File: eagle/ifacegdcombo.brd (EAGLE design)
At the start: 95.8 x 108.5 mm, 35 parts, among them K1 G5V-2, X4 BU-SMA-V

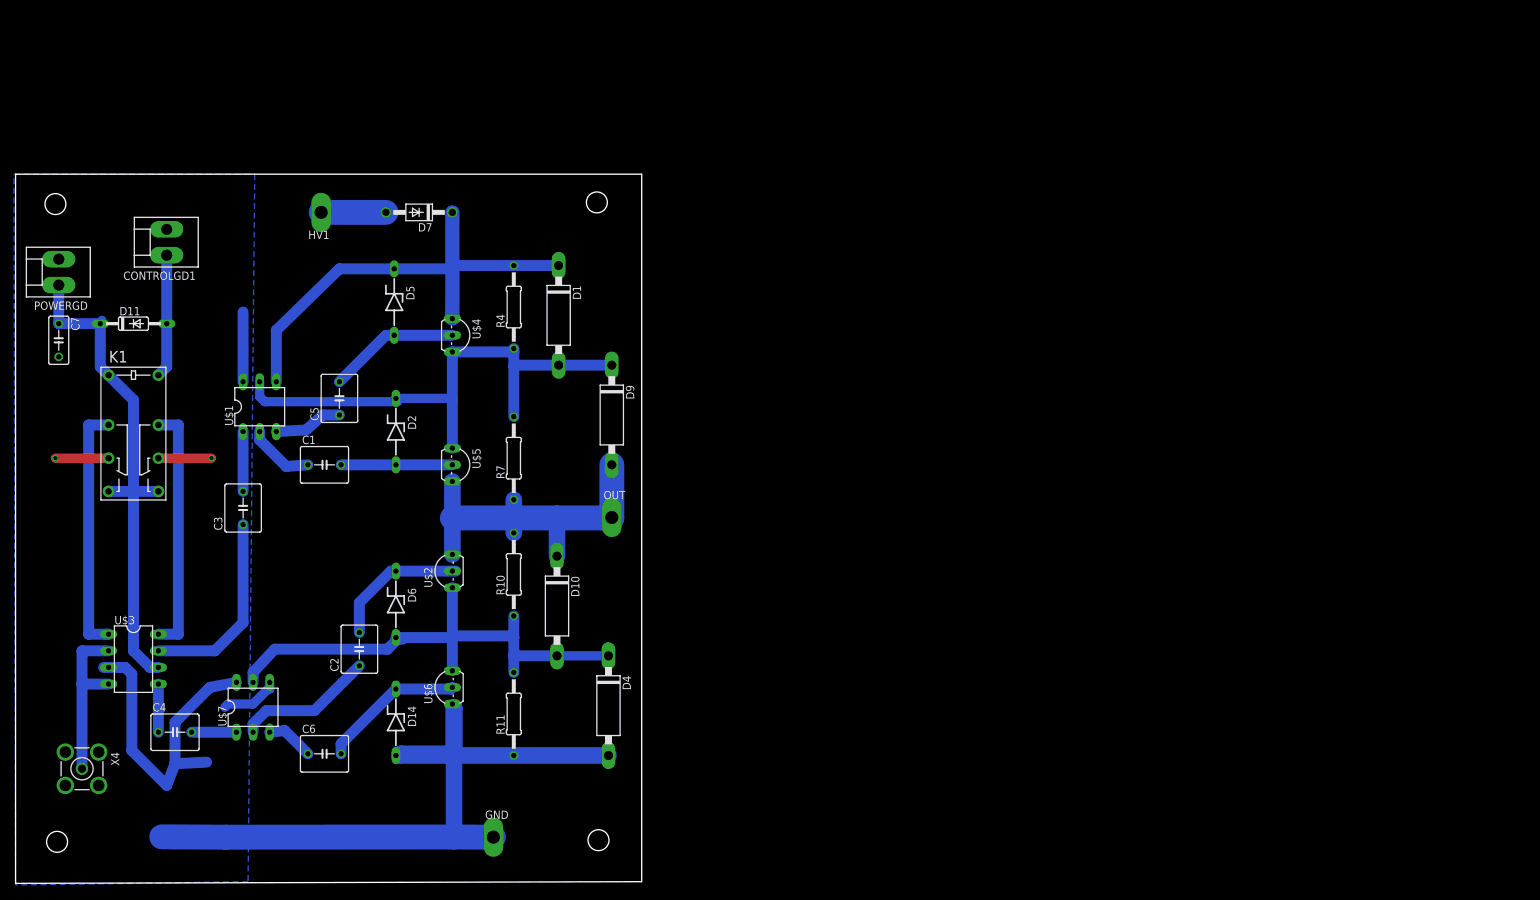
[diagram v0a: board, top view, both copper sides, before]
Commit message: 3PS, 2 1kV in parallel
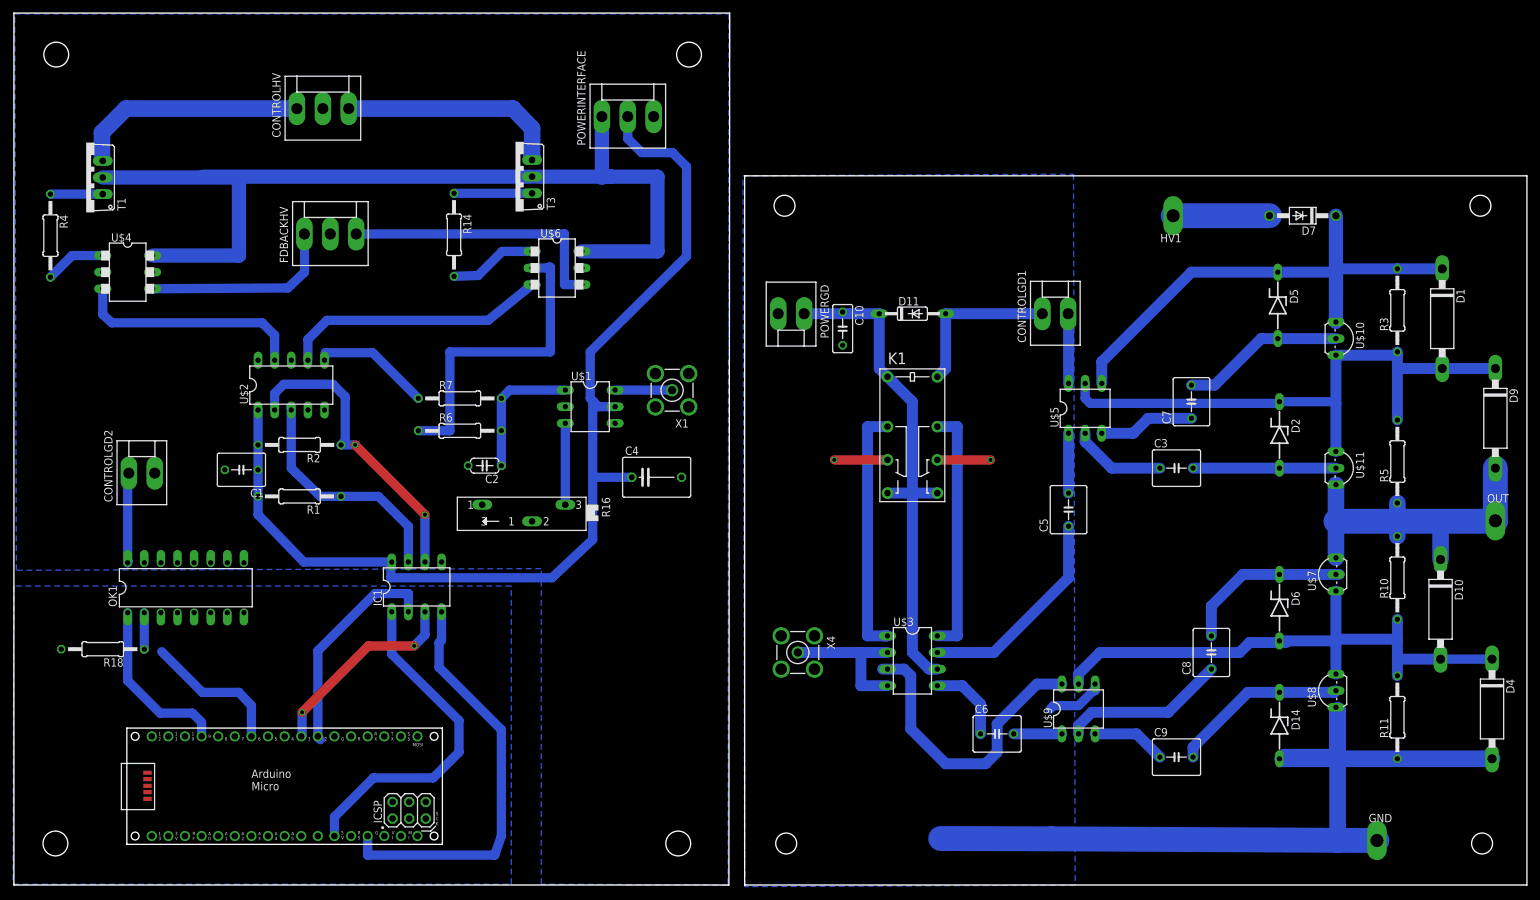
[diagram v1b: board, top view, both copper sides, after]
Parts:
- added C10: (no value), rcl:C050-030X075
- added C8, C9: (no value), resistor:C050-055X075
- added CONTROLGD2: (no value), con-molex:KK-156-2
- added CONTROLHV, FDBACKHV, POWERINTERFACE: (no value), con-molex:KK-156-3
- added IC1: ISO1540, texas:DIL08
- added OK1: PS2501", optocoupler:DIL16
- added PCB1: ARDUINO_MICRO, E14_Arduino_published:ARDUINO_MICRO
- added R1, R2: 1.5k, resistor:0207/12
- added R14: 1k, resistor:0207/12
- added R16: (no value), pot:SP19L
- added R18: 100, rcl:0207/12
- added R3, R5: 10M, rcl:0207/12
- added R6: 10k, resistor:0207/12
- added T1, T3: TIP122V, transistor-npn:TO220V
- added U$10, U$11: VP0550, transistor-fet:TO92-
- added U$8: VN0550, transistor-fet:TO92-
- added U$9: DA-2320, trafo:DIL06
- added X1: BU-SMA-V, con-coax:BU-SMA-V
- C1: device resistor:C050-055X075 -> rcl:C050-050X075
- C2: value (none) -> 10n; device resistor:C050-055X075 -> resistor:C050-024X044
- C4: device resistor:C050-055X075 -> resistor:C075-063X106
- C7: device rcl:C050-030X075 -> resistor:C050-055X075
- R4: value 10M -> 1k; device rcl:0207/12 -> resistor:0207/12
- R7: value 10M -> 40k; device rcl:0207/12 -> resistor:0207/12
- U$1: value DA-2320 -> LTC6992; device trafo:DIL06 -> linear-technology:DIL06
- U$2: value VN0550 -> MCP4728DIL; device transistor-fet:TO92- -> microchip:DIL10
- U$4: value VP0550 -> MAX9650DIL; device transistor-fet:TO92- -> maxim:DIL06-4
- U$5: value VP0550 -> DA-2320; device transistor-fet:TO92- -> trafo:DIL06
- U$6: value VN0550 -> MAX9650DIL; device transistor-fet:TO92- -> maxim:DIL06-4
- U$7: value DA-2320 -> VN0550; device trafo:DIL06 -> transistor-fet:TO92-
- moved C7 173.5 mm to (180.1, 73.9), turned to 90 degrees
- moved U$7 166.8 mm to (202.2, 47.5), turned to 90 degrees
- moved C3 142.9 mm to (177.8, 63.8), turned to 0 degrees
- moved CONTROLGD1 136.3 mm to (159.3, 87.4), turned to 0 degrees
- moved D5 135.1 mm to (193.3, 88.6)
- moved D7 135.1 mm to (197.1, 102.4)
- moved D9 135.1 mm to (226.6, 71.4)
- moved OUT 135.1 mm to (226.6, 55.7)
- moved D1 135.1 mm to (218.4, 86.6)
- moved D10 135.1 mm to (218.2, 42.2)
- moved D14 135.1 mm to (193.5, 24.4)
- moved D2 135.1 mm to (193.5, 68.8)
- moved D4 135.1 mm to (226.1, 26.9)
- moved D6 135.1 mm to (193.5, 42.4)
- moved GND 135.1 mm to (208.5, 6.81)
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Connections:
- removed net N$22: C2.1, U$7.2
- removed net N$23 (its old number): C6.1, U$7.3
- removed net N$6 (its old number): C4.2, U$7.1
- new net +12V: POWERINTERFACE.1, T1.2, T3.2, U$4.6, U$6.6
- new net A+5: IC1.1, PCB1.+5V
- new net AGND: IC1.4, PCB1.GND., R18.2
- new net D10: PCB1.D10
- new net D11: PCB1.D11
- new net D4: PCB1.D4
- new net D7: PCB1.D7
- new net D8: PCB1.D8
- new net ENSW2: CONTROLGD2.1, OK1.16
- new net GND1: C10.2, CONTROLGD1.2, D14.A, D4.A, GND.TP, K1.11, K1.6, POWERGD.2, R11.1, U$3.3, U$5.6, U$8.3, U$9.4, U$9.6, X4.2, X4.3, X4.4, X4.5
- new net N$1: R7.1, U$2.6
- new net N$10: C5.1, U$3.7
- new net N$12: R16.E, U$1.SET
- new net N$14: FDBACKHV.3, U$6.4
- new net N$15: R14.1, T3.1
- new net N$19: R4.2, U$4.1
- new net N$24: C3.1, U$5.2
- new net N$26: C8.1, U$9.2
- new net N$28: C8.2, D6.C, U$7.2
- new net N$29: C9.2, D14.C, U$8.2
- new net N$30: C3.2, D2.A, U$11.2
- new net N$31: C7.2, D5.A, U$10.2
- new net N$32: D1.C, D5.C, D7.C, R3.2, U$10.3, U$5.4
- new net N$33: D10.C, D9.A, OUT.TP, R10.2, R5.1, U$11.1, U$7.1
- new net N$35: C6.2, U$9.1
- new net N$36: U$9.5
- new net N$37: D10.A, D4.C, D6.A, R10.1, R11.2, U$7.3, U$8.1
- new net N$38: D1.A, D2.C, D9.C, R3.1, R5.2, U$10.1, U$11.3, U$5.5
- new net N$8: FDBACKHV.1, U$4.4
- new net PWM5: PCB1.D5
- new net PWM6: PCB1.D6
- new net PWM9: OK1.1, PCB1.D9
- new net SCL: IC1.3, PCB1.D3
- new net SCL_OUT: IC1.6, R2.1, U$2.2
- new net SDA: IC1.2, PCB1.D2
- new net SDA_OUT: IC1.7, R1.1, U$2.3
- new net VCC: C1.1, C4.1, IC1.8, POWERINTERFACE.2, R1.2, R2.2, U$1.VCC, U$2.1
- net +15V: now also C10.1; no longer C7.1
- net GND: now also C1.2, C2.2, C4.2, CONTROLGD2.2, CONTROLHV.2, FDBACKHV.2, IC1.5, OK1.15, POWERINTERFACE.3, R16.A, R16.S, R6.1, U$1.DIV, U$1.GND, U$2.10, U$2.4, U$4.2, U$6.2, X1.2, X1.3, X1.4, X1.5; no longer C7.2, CONTROLGD1.2, D14.A, D4.A, GND.TP, K1.11, K1.6, POWERGD.2, R11.1, U$1.6, U$3.3, U$6.3, U$7.4, U$7.6, X4.2, X4.3, X4.4, X4.5
- net N$11: now also C6.1, U$3.5; no longer C1.2, D2.A, U$5.2
- net N$13: now also U$1.OUT, X1.1; no longer D10.A, D4.C, D6.A, R10.1, R11.2, U$2.3, U$6.1
- net N$16: now also U$2.9, U$4.3; no longer C5.2, D5.A, U$4.2
- net N$17: now also U$2.8; no longer D1.C, D5.C, D7.C, R4.2, U$1.4, U$4.3
- net N$18: now also U$2.7, U$6.3; no longer D1.A, D2.C, D9.C, R4.1, R7.2, U$1.5, U$4.1, U$5.3
- net N$2: now also C2.1, R6.2, R7.2, U$1.MOD; no longer C3.1, U$3.7
- net N$21: now also R14.2, U$6.1; no longer D10.C, D9.A, OUT.TP, R10.2, R7.1, U$2.1, U$5.1
- net N$25: now also C7.1, U$5.3; no longer C2.2, D6.C, U$2.2
- net N$27: now also C9.1, U$9.3; no longer C6.2, D14.C, U$6.2
- net N$3: now also R4.1, T1.1; no longer C3.2, U$1.1
- net N$4: now also CONTROLHV.1, T1.3; no longer C4.1, U$3.5
- net N$5: now also CONTROLHV.3, T3.3; no longer C1.1, U$1.2
- net N$7: now also OK1.2, R18.1; no longer C5.1, U$1.3
- net N$9: now also C5.2, U$5.1; no longer U$7.5
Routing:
- net GND1: track 0.00 -> 215.9 mm, vias 0 -> 2
- net VCC: track 0.00 -> 162.9 mm
- net GND: track 204.5 -> 48.1 mm, vias 2 -> 0
- net +12V: track 0.00 -> 149.3 mm
- net N$38: track 0.00 -> 90.7 mm
- net N$32: track 0.00 -> 85.7 mm
- net N$17: track 79.5 -> 0.00 mm
- net AGND: track 0.00 -> 63.8 mm
- net N$37: track 0.00 -> 55.6 mm
- net N$33: track 0.00 -> 54.6 mm
- net A+5: track 0.00 -> 51.8 mm
- net N$13: track 55.6 -> 8.72 mm
- net SCL_OUT: track 0.00 -> 46.8 mm, vias 0 -> 2
- net N$14: track 0.00 -> 42.3 mm
- net N$18: track 82.5 -> 40.6 mm
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- added copper zone on layer 16, net AGND
- added copper zone on layer 16, net GND1
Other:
- board size 95.8 x 108.5 mm -> 231.4 x 133.3 mm

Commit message: IXYS board solution, gatedriver components
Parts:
- removed D7: 1N4004, diode:DO41-10
- removed GND: TPPAD1-20Y, testpad:P1-20Y
- removed OK1: PS2501", optocoupler:DIL16
- added C11: (no value), rcl:C050-050X075
- added C12: 10n, resistor:C050-024X044
- added HV2: TPPAD1-20Y, testpad:P1-20Y
- added OK2: H11F1, optocoupler:DIL05
- added R12, R13, R8, R9: 70, rcl:0207/10
- added R15: 10k, resistor:0207/12
- added R17: 40k, resistor:0207/12
- added R19, R20: 1.5k, resistor:0207/12
- added R21, R22: 1k, resistor:0207/12
- C1: value (none) -> .22u; device rcl:C050-050X075 -> resistor:C050-055X075
- C10: device rcl:C050-030X075 -> resistor:C075-063X106
- C2: value 10n -> .22u; device resistor:C050-024X044 -> resistor:C050-055X075
- C3, C5, C6: value (none) -> .22u
- C4: value (none) -> .22u; device resistor:C075-063X106 -> resistor:C050-055X075
- C7: device resistor:C050-055X075 -> rcl:C050-030X075
- C8, C9: value (none) -> 10p; device resistor:C050-055X075 -> resistor:C102-064X133
- R1, R2: value 1.5k -> 50k; device resistor:0207/12 -> rcl:0207/10
- R10, R11: value 10M -> 1M; device rcl:0207/12 -> rcl:0207/10
- R14, R4: value 1k -> 1M; device resistor:0207/12 -> rcl:0207/10
- R3, R5: value 10M -> 50k; device rcl:0207/12 -> rcl:0207/10
- R6: value 10k -> 70; device resistor:0207/12 -> rcl:0207/10
- R7: value 40k -> 1M; device resistor:0207/12 -> rcl:0207/10
- U$1: value LTC6992 -> DA-2320; device linear-technology:DIL06 -> trafo:DIL06
- U$10, U$11: value VP0550 -> MAX9650DIL; device transistor-fet:TO92- -> maxim:DIL06-4
- U$2: value MCP4728DIL -> VN0550L; device microchip:DIL10 -> transistor-fet:TO92L
- U$4: value MAX9650DIL -> VP0550L; device maxim:DIL06-4 -> transistor-fet:TO92L
- U$5: value DA-2320 -> VP0550L; device trafo:DIL06 -> transistor-fet:TO92L
- U$6: value MAX9650DIL -> VN0550L; device maxim:DIL06-4 -> transistor-fet:TO92L
- U$7: value VN0550 -> DA-2320; device transistor-fet:TO92- -> trafo:DIL06
- U$8: value VN0550 -> LTC6992; device transistor-fet:TO92- -> linear-technology:DIL06
- U$9: value DA-2320 -> MCP4728DIL; device trafo:DIL06 -> microchip:DIL10
- moved C7 173.5 mm to (6.86, 83.3), turned to 270 degrees
- moved U$7 168.9 mm to (34.5, 27.2), turned to 0 degrees
- moved R3 152.4 mm to (66.0, 42.7), turned to 270 degrees
- moved R5 151.0 mm to (66.3, 23.6), turned to 270 degrees
- moved C8 143.7 mm to (56.1, 102.9), turned to 180 degrees
- moved C3 143.6 mm to (35.1, 48.5), turned to 90 degrees
- moved D6 137.7 mm to (55.9, 42.7)
- moved D14 137.4 mm to (56.1, 23.6)
- moved D2 137.2 mm to (56.4, 69.3)
- moved D5 136.9 mm to (56.4, 89.4)
- moved CONTROLGD1 136.3 mm to (23.4, 98.3), turned to 90 degrees
- moved D4 130.1 mm to (96.0, 26.2)
- moved D9 130.0 mm to (96.5, 71.6)
- moved OUT 130.0 mm to (96.5, 56.0)
- moved R11 128.5 mm to (83.1, 23.6)
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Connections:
- removed net N$1 (its old number): R7.1, U$2.6
- removed net N$14 (its old number): FDBACKHV.3, U$6.4
- removed net N$15 (its old number): R14.1, T3.1
- new net N$20: C4.2, R14.2
- new net N$22: C2.1, U$7.2
- new net N$23: C6.1, U$7.3
- new net N$251: R3.1, R9.2, U$2.2
- new net N$39: R22.2, U$11.1
- new net N$4: C4.1, U$3.5
- new net N$43: R21.1, T1.1
- new net N$5: C1.1, U$1.2
- new net N$6: R14.1, U$7.1
- net +12V: now also U$10.6, U$11.6; no longer U$4.6, U$6.6
- net +15V: now also C7.1; no longer C10.1
- net ENSW2: now also OK2.6; no longer OK1.16
- net GND: now also C7.2, C8.2, C9.2, CONTROLGD1.2, K1.11, K1.6, POWERGD.2, U$1.6, U$3.3, U$7.6, X4.2, X4.3, X4.4, X4.5; no longer C1.2, C2.2, C4.2, CONTROLGD2.2, CONTROLHV.2, FDBACKHV.2, IC1.5, OK1.15, POWERINTERFACE.3, R16.A, R16.S, R6.1, U$1.DIV, U$1.GND, U$2.10, U$2.4, U$4.2, U$6.2, X1.2, X1.3, X1.4, X1.5
- net GND1: now also C11.2, C12.2, CONTROLGD2.2, CONTROLHV.2, FDBACKHV.2, IC1.5, OK2.4, POWERINTERFACE.3, R15.1, R16.A, R16.S, U$10.2, U$11.2, U$8.DIV, U$8.GND, U$9.10, X1.2, X1.3, X1.4, X1.5; no longer CONTROLGD1.2, D14.A, D4.A, GND.TP, K1.11, K1.6, POWERGD.2, R11.1, U$3.3, U$5.6, U$8.3, U$9.6, X4.2, X4.3, X4.4, X4.5
- net N$10: now also C1.2, D2.A, R6.1; no longer C5.1, U$3.7
- net N$11: now also R12.2, R5.1, U$6.2; no longer C6.1, U$3.5
- net N$12: now also R2.1, R8.2, U$4.2; no longer R16.E, U$1.SET
- net N$13: now also D10.A, D4.C, D6.A, R10.1, R11.2, R3.2, U$2.3, U$6.1; no longer U$1.OUT, X1.1
- net N$16: now also C5.2, D5.A, R8.1; no longer U$2.9, U$4.3
- net N$17: now also C8.1, D1.C, D5.C, HV1.TP, R2.2, R4.2, U$1.4, U$4.3; no longer U$2.8
- net N$18: now also D1.A, D2.C, D9.C, R1.2, R4.1, R7.2, U$1.5, U$4.1, U$5.3; no longer U$2.7, U$6.3
- net N$19: now also C3.2, R13.2; no longer R4.2, U$4.1
- net N$2: now also C3.1, U$3.7; no longer C2.1, R6.2, R7.2, U$1.MOD
- net N$21: now also D10.C, D9.A, OUT.TP, R10.2, R7.1, U$2.1, U$5.1; no longer R14.2, U$6.1
- net N$24: now also C9.1, D14.A, D4.A, HV2.TP, R11.1, R5.2, U$6.3, U$7.4; no longer C3.1, U$5.2
- net N$25: now also C2.2, D6.C, R9.1; no longer C7.1, U$5.3
- net N$26: now also R16.E, U$8.SET; no longer C8.1, U$9.2
- net N$27: now also C6.2, D14.C, R12.1; no longer C9.1, U$9.3
- net N$28: now also U$8.OUT, X1.1; no longer C8.2, D6.C, U$7.2
- net N$29: now also OK2.1, R18.1; no longer C9.2, D14.C, U$8.2
- net N$3: now also R13.1, U$1.1; no longer R4.1, T1.1
- net N$30: now also C12.1, R15.2, R17.2, U$8.MOD; no longer C3.2, D2.A, U$11.2
- net N$31: now also FDBACKHV.1, U$10.4; no longer C7.2, D5.A, U$10.2
- net N$32: now also FDBACKHV.3, U$11.4; no longer D1.C, D5.C, D7.C, R3.2, U$10.3, U$5.4
- net N$33: now also U$10.3, U$9.9; no longer D10.C, D9.A, OUT.TP, R10.2, R5.1, U$11.1, U$7.1
- net N$34: now also U$9.8; no longer D7.A, HV1.TP
- net N$35: now also U$11.3, U$9.7; no longer C6.2, U$9.1
- net N$36: now also R17.1, U$9.6; no longer U$9.5
- net N$37: now also R22.1, T3.1; no longer D10.A, D4.C, D6.A, R10.1, R11.2, U$7.3, U$8.1
- net N$38: now also R21.2; no longer D1.A, D2.C, D9.C, R3.1, R5.2, U$11.3, U$5.5
- net N$7: now also C5.1, U$1.3; no longer OK1.2, R18.1
- net N$8: now also R1.1, R6.2, U$5.2; no longer FDBACKHV.1, U$4.4
- net N$9: now also U$7.5; no longer C5.2, U$5.1
- net PWM9: now also OK2.2; no longer OK1.1
- net SCL_OUT: now also R20.1, U$9.2; no longer R2.1, U$2.2
- net SDA_OUT: now also R19.1, U$9.3; no longer R1.1, U$2.3
- net VCC: now also C10.1, C11.1, R19.2, R20.2, U$8.VCC, U$9.1; no longer C1.1, C4.1, R1.2, R2.2, U$1.VCC, U$2.1
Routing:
- net GND1: track 215.9 -> 38.7 mm, vias 2 -> 0
- net N$17: track 0.00 -> 98.4 mm
- net AGND: track 63.8 -> 159.2 mm
- net N$38: track 90.7 -> 9.37 mm
- net N$24: track 14.4 -> 95.6 mm
- net +12V: track 149.3 -> 84.8 mm
- net N$18: track 40.6 -> 100.8 mm
- net N$13: track 8.72 -> 68.3 mm
- net N$32: track 85.7 -> 33.8 mm
- net GND: track 48.1 -> 98.9 mm, vias 0 -> 2
- net N$37: track 55.6 -> 11.9 mm
- net N$21: track 13.5 -> 56.6 mm
- net N$14 (its old number): track 42.3 -> 0.00 mm
- net A+5: track 51.8 -> 91.0 mm
- net N$33: track 54.6 -> 22.4 mm
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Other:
- board size 231.4 x 133.3 mm -> 192.8 x 133.3 mm
